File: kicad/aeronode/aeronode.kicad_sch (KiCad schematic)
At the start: 73 parts, among them J1 IMU_BOARD, J2 USB-C PD / recovery, J3 2S LiFePO4 6Ah + BMS, Q1 NMOS pass - TBD, SW1 ON/OFF, U1 ConnectCore93_LGA, U10 BMP390, U2 CYPD3177-24LQ, U3 BQ25798, U4 LMR33630ADDA, U5 LTC4364CMS, U6 BME690, U7 DAN-F10N, U9 MMC5983MA

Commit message: [LIMA] kicad: verify MMC5983MA land pattern, assign stock LGA-16 to U9
Measured MEMSIC's own land drawing (Rev A p20) against KiCad's stock
Package_LGA:LGA-16_3x3mm_P0.5mm. Exact match on pad size (0.45x0.30),
radial offset (1.275), pitch (0.5) and body (3x3) - assigned as-is, no
authoring needed. The stock footprint cites sibling part MMC5883MA, so it
was drawn from a MEMSIC drawing rather than guessed; verified anyway.

Caught a misreading that would have shipped: the drawing's 2.550 is
centre-to-centre, not outer-edge to outer-edge. The outer-edge reading
gives 1.050 vs the true 1.275 - 0.225mm wrong on all 16 pads.

Also recorded MEMSIC's explicit p12 placement rule (no current-carrying
traces under the sensor or on the opposite side of the board), which
strengthens the case for moving U9 to the imu-board.

Footprints now 82 of 83; only U10 BMP390 remains.

Co-Authored-By: Claude Opus 5 <noreply@anthropic.com>
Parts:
- U9: footprint (none) -> Package_LGA:LGA-16_3x3mm_P0.5mm
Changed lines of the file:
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@@
 			)
 		)
-		(property "Footprint" ""
+		(property "Footprint" "Package_LGA:LGA-16_3x3mm_P0.5mm"
 			(at 1060.45 539.75 0)
 			(hide yes)

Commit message: [LIMA] kicad: author BMP390 footprint, all 83 footprints now assigned
Rejected ST_HLGA-10_2x2mm_P0.5mm_LayoutBorder3x2y: it is ST's LPS22HH pattern
with a 3-2-3-2 pad layout and 0.425x0.35 pads. The BMP390 is 2-3-2-3 with
0.275x0.250 pads - same envelope and same 0.7625 radial offset, different part.
It would have looked placed and would not have soldered.

Bosch publish no separate land pattern; datasheet 7.2 directs using the package
outline dimensions as the landing pattern, so copper is 1:1 with the package pads.
Geometry closes exactly: 0.7625 + 0.1375 + 0.100 = 1.000 = half the 2.00 package,
across three independently-stated dimensions - built from the numbers rather than
measured off the bitmap. Built file reproduces it (max extent 0.9000, gap 0.100).

Drawn in top view per Fig 23, so pin 1 (VDDIO) is at TOP RIGHT by design, keeping
the footprint comparable to the datasheet figure. F.Fab marks the 0.25mm port hole
at (+0.40,-0.40), which must not be obstructed.

Verified: 10/10 pads vs Fig 23, 10/10 symbol pins vs Table 52, 0 overlaps, min
copper gap 0.250mm. ERC unchanged at 186 pre-existing violations.

Footprint assignment complete: 83 of 83.

Co-Authored-By: Claude Opus 5 <noreply@anthropic.com>
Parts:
- U10: footprint (none) -> Bosch:Bosch_BMP390_LGA-10_2x2mm
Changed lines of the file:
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@@
 			)
 		)
-		(property "Footprint" ""
+		(property "Footprint" "Bosch:Bosch_BMP390_LGA-10_2x2mm"
 			(at 1060.45 459.74 0)
 			(hide yes)

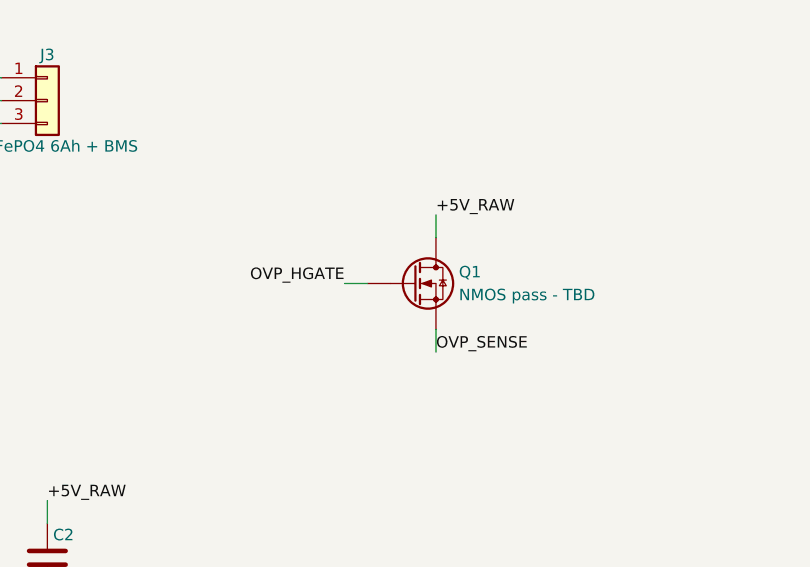
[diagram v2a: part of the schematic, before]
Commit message: [LIMA] kicad: import netlist to PCB, draw 90x70 outline, fix unconnectable Q1
Netlist import: 73 footprints, 385 nets. kicad-cli has no update-pcb-from-schematic
and KiCad 10's pcbnew SWIG exposes no BOARD_NETLIST_UPDATER, so this is a scripted
import verified by re-reading the saved board: 806 nodes checked, 0 mismatches, and
kicad-cli pcb drc reports schematic_parity 0.

Q1 could never have worked. It used Device:Q_NMOS, whose pin NUMBERS are the letters
D/G/S, against a SOT-23 footprint with pads 1/2/3 - all three pads bound to nothing,
so the OVP pass FET was electrically absent. ERC cannot see this; it only exists at
the symbol/footprint boundary. KiCad 10 ships no Q_NMOS_* numbered variants, so
authored AeroNode:NMOS_GSD (Q_NMOS graphics, pins 1=G/2=S/3=D). Not patched into the
schematic's cached lib_symbols, which Update-Symbols-from-Library would revert.

Outline 90x70mm, R3 corners, 4x M3 NPTH on an 80x60 pattern. Size is an ASSUMPTION -
3010mm2 of courtyard over 73 parts gives ~48% density. Cheap to change now, not later.
Anchors placed: CC93, GNSS top-right (sky view, away from switchers), IMU header on
the right edge, USB-C flush with the bottom edge, battery bottom-centre.

Two placement errors caught by measurement, not inspection: J1 rotated 90deg landed
18.7mm off the board (its native courtyard is already tall), and J3 hung 0.89mm past
the edge because a pin header's origin is pin 1, not the courtyard centre. Placement
now targets courtyard centres.

DRC 0 violations. Fixed U10's 0.7mm silk text. Accepted one residual via a rule scoped
to J2 only: the USB-C receptacle's own GND holes sit 0.1847mm from its own NPTH holes,
fixed by the connector's mechanics. Fab must confirm 0.18mm hole-to-hole.

Also corrected the record: 73 components, not 83 - the old number counted symbol units
and U1 is an 11-unit symbol.

Co-Authored-By: Claude Opus 5 <noreply@anthropic.com>
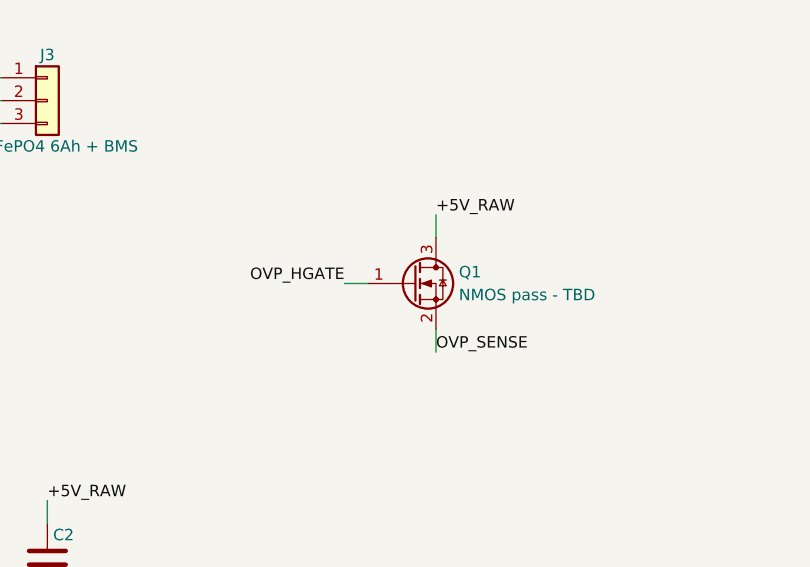
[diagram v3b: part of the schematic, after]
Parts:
- Q1: symbol Device:Q_NMOS -> AeroNode:NMOS_GSD
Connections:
- net +5V_RAW: now also Q1.3 (D); no longer Q1.D
- net OVP_HGATE: now also Q1.1 (G); no longer Q1.G
- net OVP_SENSE: now also Q1.2 (S); no longer Q1.S
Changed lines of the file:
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@@
 	)
 	(symbol
-		(lib_id "Device:Q_NMOS")
+		(lib_id "AeroNode:NMOS_GSD")
 		(at 800.1 640.08 0)
 		(unit 1)

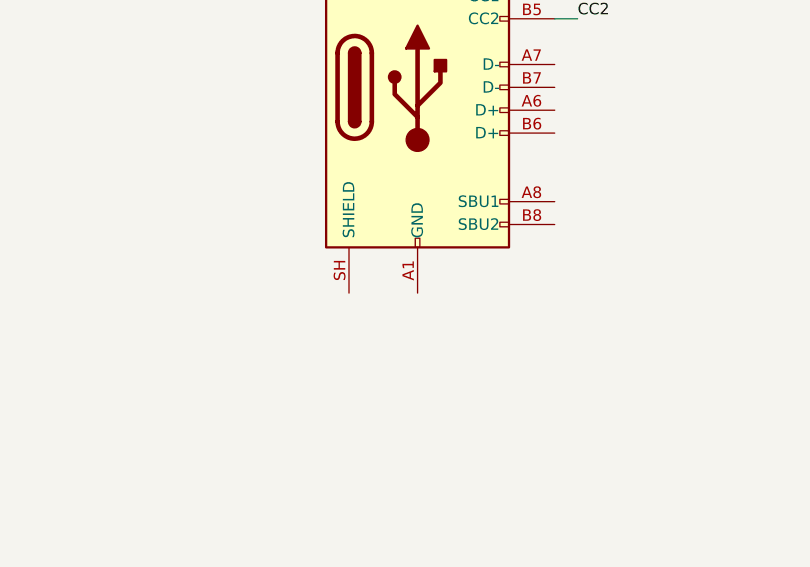
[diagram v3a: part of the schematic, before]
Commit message: [LIMA] kicad: FIX - USB-C ground was never connected to system GND
J2's four GND pins (A1/A12/B1/B12) are stacked on one connection point in the
USB_C_Receptacle_USB2.0_16P symbol, so they formed their own 4-node net
'Net-(J2-GND-PadA1)' with no wire and no label attaching them to /GND. The
SHIELD pin was likewise floating. /GND had 254 nodes and J2 was not among them.

Impact if built: VBUS arrives with no return path. No charging, no PD
negotiation, CC1/CC2 with no ground reference - the board is dead on USB.

ERC did not surface it usefully: the pins are connected to EACH OTHER, so they
are not 'unconnected pins', and the design already carries 170 pin_not_connected
warnings from unused CC93 pads, which buries anything real. It was found by
inspecting net pad-counts while planning the ground plane.

Fix: added GND labels at (149.86,642.62) and (142.24,642.62) - this schematic
uses local labels, not power symbols, so that is the idiomatic form here.
/GND now 259 nodes with J2 A1/A12/B1/B12/SH present, no isolated J2 nets.
Board re-bound from the corrected netlist: 8 pads changed, 0 mismatches,
DRC 0 violations, schematic parity 0.

Shield is tied directly to GND. Standard for a board with no separate chassis
ground, but revisit if the enclosure needs a decoupled shield connection.

Co-Authored-By: Claude Opus 5 <noreply@anthropic.com>
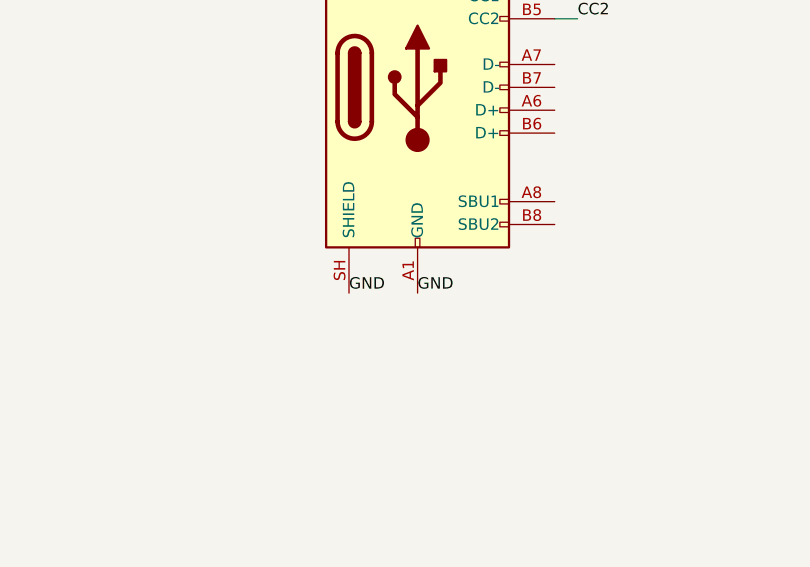
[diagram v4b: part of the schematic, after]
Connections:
- net GND: now also J2.A1 (GND), J2.A12 (GND), J2.B1 (GND), J2.B12 (GND), J2.SH (SHIELD)
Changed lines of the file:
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@@
+		)
+	)
+	(label "GND"
+		(at 149.86 642.62 0)
+		(effects
+			(font
+				(size 1.27 1.27)
+			)
+			(justify left bottom)
+		)
+	)
+	(label "GND"
+		(at 142.24 642.62 0)
+		(effects
+			(font
+				(size 1.27 1.27)
+			)
+			(justify left bottom)
 		)
 	)
